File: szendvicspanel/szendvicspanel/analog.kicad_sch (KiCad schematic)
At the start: 0 parts

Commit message: Jack és magas szintű terv
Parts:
- added J1: AudioJack4, Connector_Audio:Jack_3.5mm_CUI_SJ1-3514N_Horizontal, symbol Connector_Audio:AudioJack4
- added R5, R6: R, symbol Device:R
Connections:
- net GND: now also J1.R2, R5.1, R6.2
- new net: J1.R1, R6.1
- new net: J1.S, R5.2
- new net JACK_INPUT: J1.T
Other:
- note added: "GND"
- note added: "LEFT"
- note added: "RC filter?"
- note added: "RIGHT"
- note added: "SLEEVE/MIC"
- note added: "erősítés"
- note added: "zajszűrés"
- note removed: "INPUT: Jack"

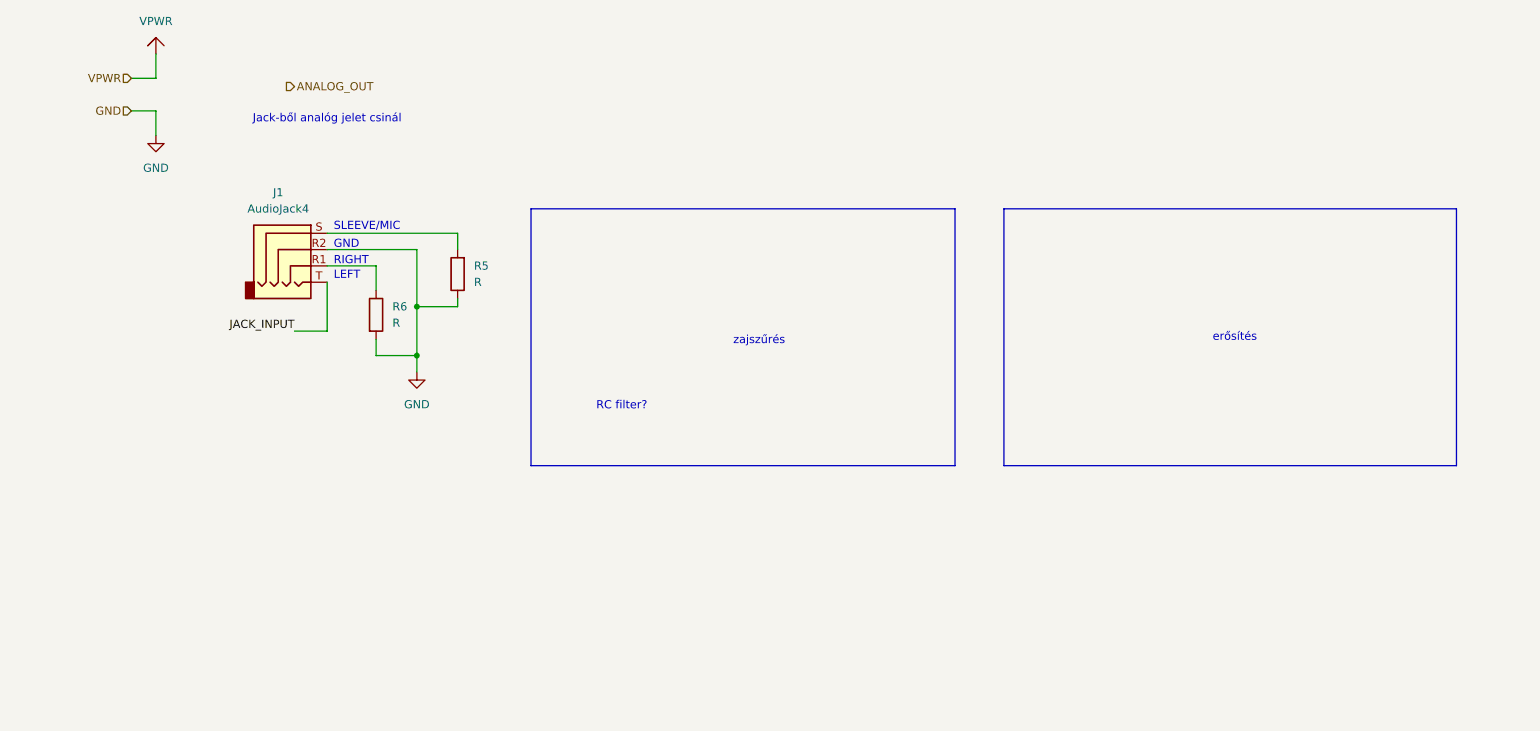
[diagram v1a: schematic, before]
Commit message: KiCAD analóg interfész
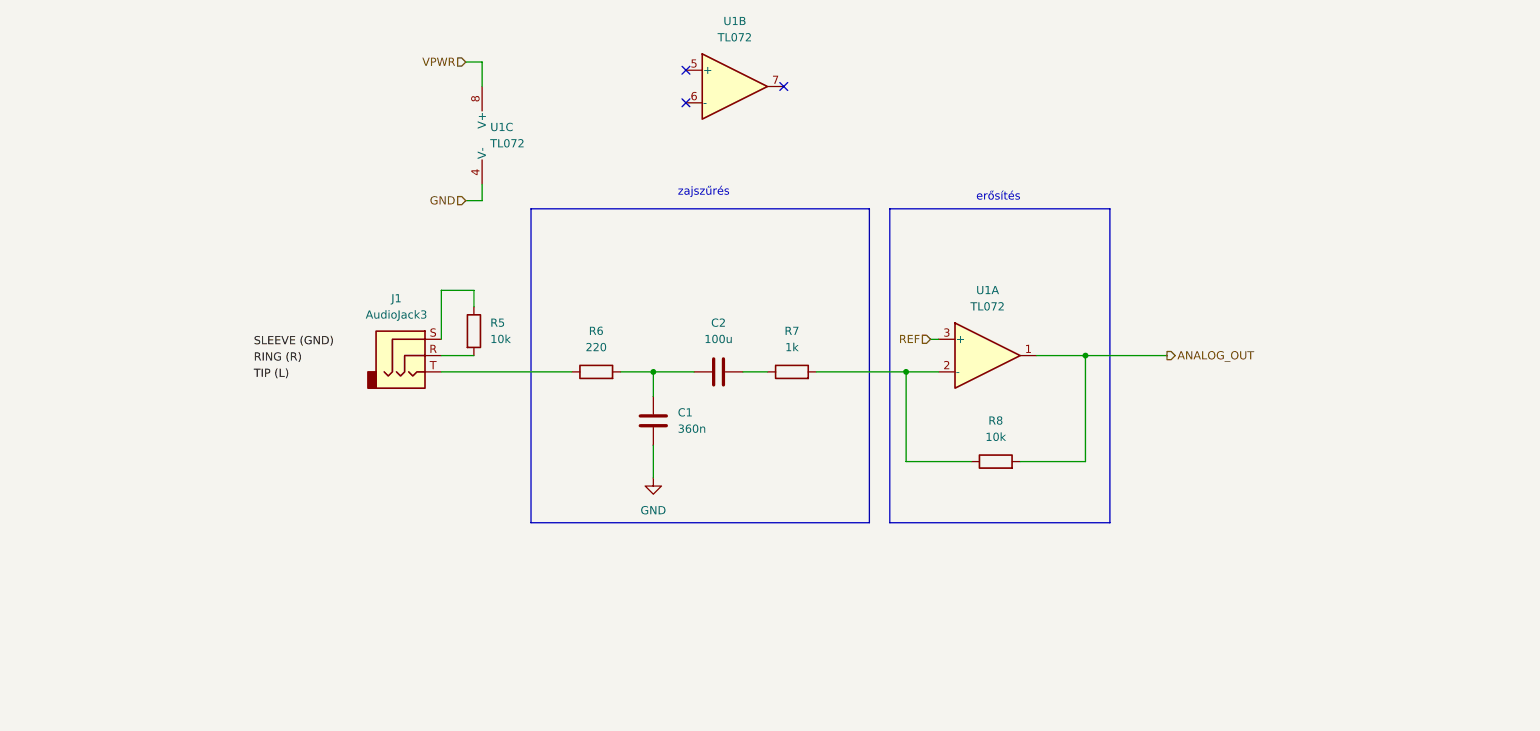
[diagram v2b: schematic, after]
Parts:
- removed J1: AudioJack4, Connector_Audio:Jack_3.5mm_CUI_SJ1-3514N_Horizontal, symbol Connector_Audio:AudioJack4
- added C1: 360n, symbol Device:C
- added C2: 100u, symbol Device:C
- added J1: AudioJack3, symbol Connector_Audio:AudioJack3
- added R7: 1k, symbol Device:R
- added R8: 10k, symbol Device:R
- added U1: TL072, symbol Amplifier_Operational:TL072
- R5: value R -> 10k
- R6: value R -> 220
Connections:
- net ANALOG_OUT: now also R8.2, U1.1
- net GND: now also C1.2, U1.4 (V-); no longer R5.1, R6.2
- net VPWR: now also U1.8 (V+)
- net at R6.1: now also J1.T
- net at R5.2: now also J1.R
- new net: C1.1, C2.2, R6.2
- new net: C2.1, R7.1
- new net: R7.2, R8.1, U1.2 (-)
- new net: J1.S, R5.1
- new net REF: U1.3 (+)
- no-connect marks 0 -> 3
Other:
- note removed: "GND"
- note removed: "Jack-ből analóg jelet csinál"
- note removed: "LEFT"
- note removed: "RC filter?"
- note removed: "RIGHT"
- note removed: "SLEEVE/MIC"
- title: (none) -> Analóg jack interfész

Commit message: Analóg jelgen schematic copy+paste, output busz, analóg interfész pinjeinek frissítése
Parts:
- added J4, J5: Conn_01x04_Pin, Connector_PinHeader_2.54mm:PinHeader_1x04_P2.54mm_Horizontal, symbol Connector:Conn_01x04_Pin
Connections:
- net ANALOG_OUT: now also J5.2 (Pin_2)
- net GND: now also J4.1 (Pin_1), J5.1 (Pin_1)
- net VPWR: now also J4.4 (Pin_4), J5.4 (Pin_4)
- net REF renamed REF_IN
- new net +5V_IN: J4.3 (Pin_3), J5.3 (Pin_3)
- new net X: J4.2 (Pin_2)
- no-connect marks 3 -> 4
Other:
- note added: "TODO: több láb kell? / saját ref előállítása?"

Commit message: Dokumentáció, Bandpass WIP
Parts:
- removed R5: 10k, symbol Device:R
- removed U1: TL072, symbol Amplifier_Operational:TL072
- added R10, R9: 220, symbol Device:R
- added RV4: R_Potentiometer, symbol Device:R_Potentiometer
- added U3: TL072, Package_DIP:DIP-8_W7.62mm, symbol Amplifier_Operational:TL072
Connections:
- net ANALOG_OUT: now also U3.1
- net GND: now also J1.S, RV4.3, U3.4 (V-)
- net VPWR: now also RV4.1, U3.8 (V+)
- net at R6.1: now also R10.2, R9.2; no longer J1.T
- net at R7.2, R8.1: now also U3.2 (-)
- net at J1.R: now also R9.1
- new net: J1.T, R10.1
- new net: RV4.2, U3.3 (+)
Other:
- note added: "bemeneti csatornák kombinálása"
- note added: "~8V referencia fesz."
- note removed: "TODO: több láb kell? / saját ref előállítása?"
- moved on the sheet: C1, C2, J1, R6, R7, R8
